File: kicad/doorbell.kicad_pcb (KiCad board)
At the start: 4 copper layers, 40.4 x 47.5 mm, 38 parts, among them J1 USB-C (USB4085), J2 WF26 (6-way screw), K1 G6K-2F-Y 4.5V, K2 G6K-2F-Y 4.5V, Q1 2N7002, Q2 2N7002, SW1 BOOT, SW2 EN, U1 ESP32-C3-WROOM-02-N4, U2 SGM2212-3.3

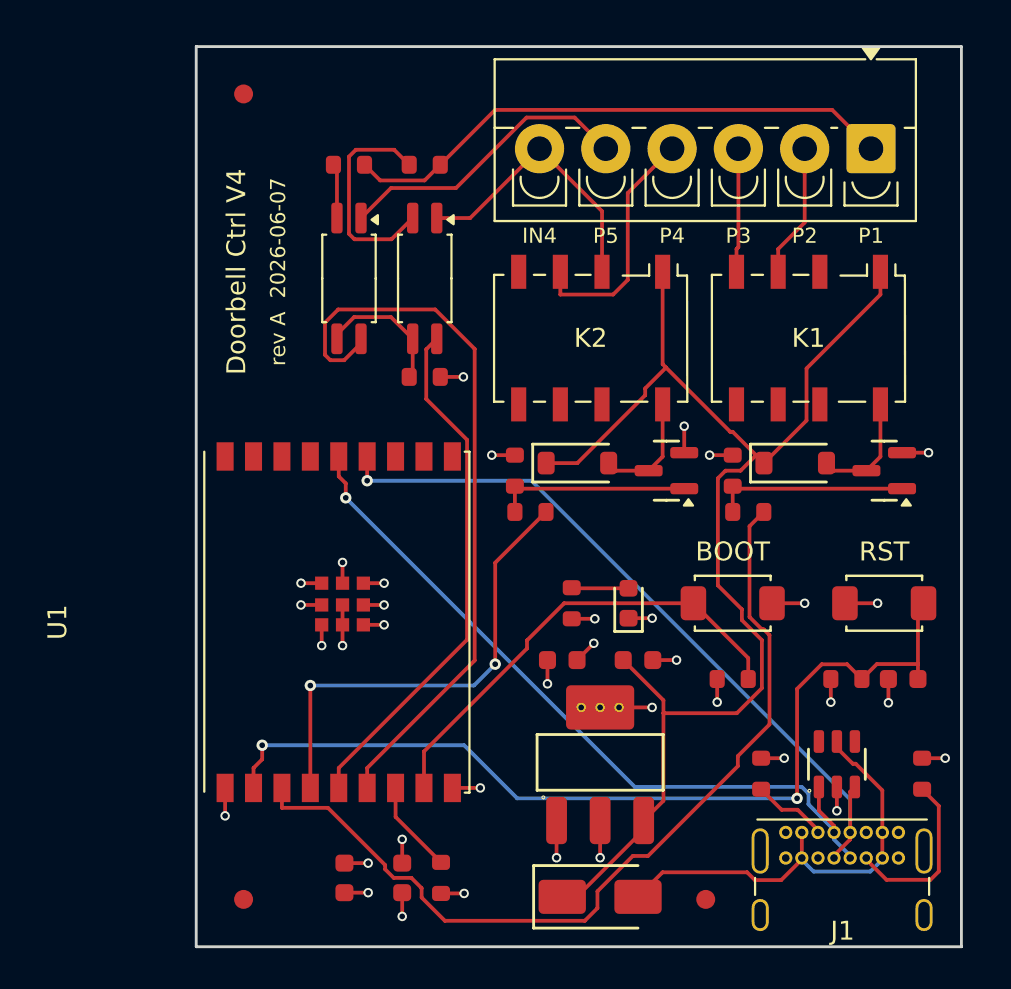
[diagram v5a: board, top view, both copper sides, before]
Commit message: Move bell sense to IO10/IO3 (opto-facing); doc + BOM update for WROOM-02
Reassign OC1_OUT/OC2_OUT from IO6/IO7 to IO10/IO3 so they land on U1's
north castellated row facing the optos: OC1/OC2 now route ~7mm straight
instead of ~25mm around the module. Non-strapping pins; IO6/IO7 freed to
No-Connect. ESPHome updated (House GPIO6->GPIO10, Apartment GPIO7->GPIO3).
Routes 0 unrouted, DRC 0/0, check_pcb PASS.

BOM: U1 LCSC C2838502 (MINI-1) -> C2934560 (WROOM-02-N4).

Docs brought in line with the WROOM-02 swap:
- DESIGN.md: GPIO map, decisions/BOM tables, floorplan, antenna overhang
  (5.9mm), and a 2026-06-08 "changes since review" addendum.
- ORDERING.md: switched the order story to Economic PCBA (no $25/side
  setup; Economic has no >=70mm/rail requirement -- that was Standard);
  updated cost, part-placement table, and the rationale.
- doorbell-v4.yaml + design comments: MINI-1 -> WROOM-02.
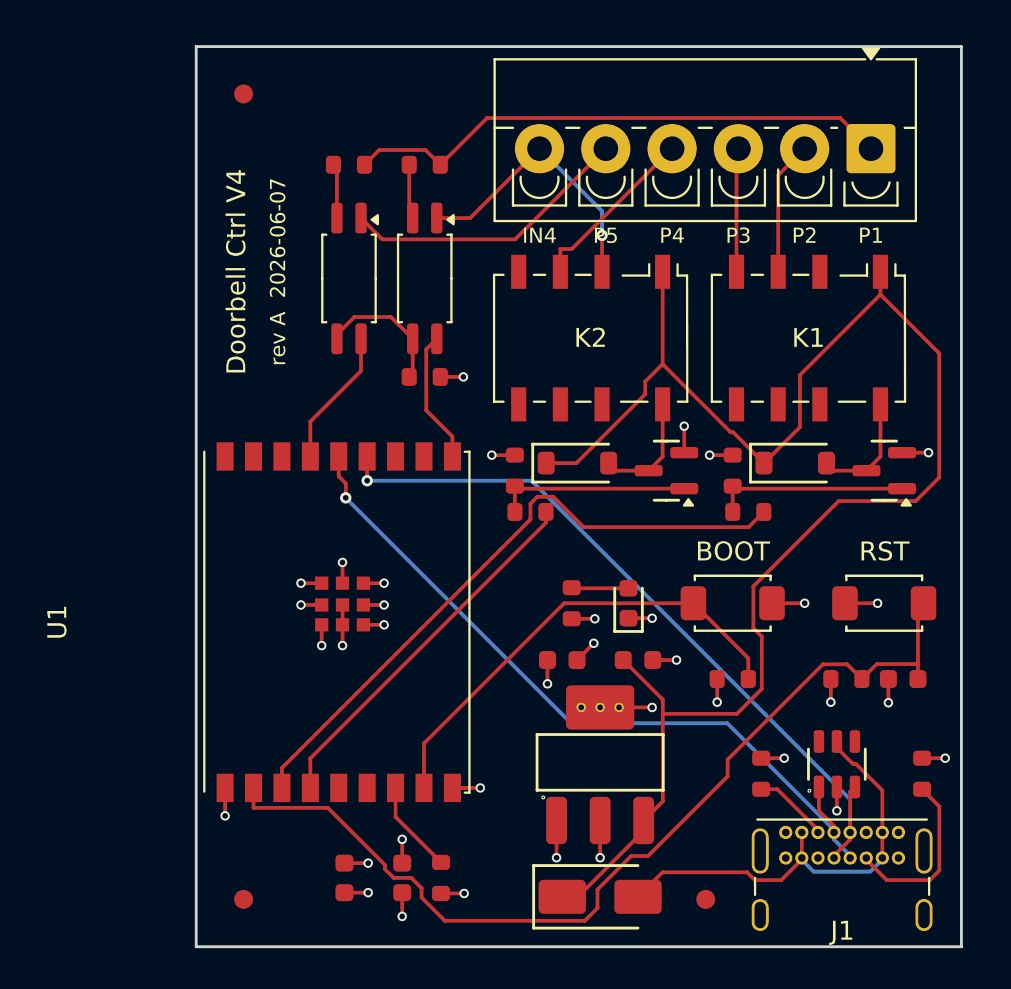
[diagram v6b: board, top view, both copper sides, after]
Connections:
- U1 pad 10: (no net) -> OC1_OUT
- U1 pad 15: (no net) -> OC2_OUT
- U1 pad 5: OC1_OUT -> (no net)
- U1 pad 6: OC2_OUT -> (no net)
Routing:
- net OC2_OUT: track 38.9 -> 7.32 mm
- net OC1_OUT: track 27.6 -> 7.01 mm
- net +5V: track 70.0 -> 84.3 mm
- net GATE1_DRV: track 46.8 -> 33.9 mm
- net OC1_CATH: track 11.7 -> 2.89 mm
- net GATE2_DRV: track 24.8 -> 19.7 mm, vias 2 -> 0
- net P4: track 13.0 -> 9.30 mm
- net EN: track 49.3 -> 50.5 mm, vias 2 -> 0
- net IN_P4: vias 0 -> 1

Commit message: Reverse-engineer WF26 handset; document bus protocol; R_em placement
- wf26/: new standalone KiCad project (ERC-clean) fully tracing the STR
  WF26/G handset internals -- LS1, S1/S2 (DPDT), R1, C1, custom HJR-4102
  relay symbol, 5-way bus. Built via make_wf26.py (kiutils bootstrap).
- DESIGN.md: WF26 internal-trace section + netlist; key finding that P4
  is dual-purpose (Tueruf ring AND Sprechen/Hoeren PTT/on-hook handshake),
  talk=P4<->P2 / listen=P4<->P3, relay-part caveat, open questions.
- docs/HJR4102.PDF: relay datasheet (6-pin DIL SPDT, coil 5/8, COM 1+12).
- kicad/: R_em (R3) re-placed/rotated 180 in gen_pcb.py + regenerated
  board/sch/pdf; add fabrication-toolkit-options.json. Ignore .history/.
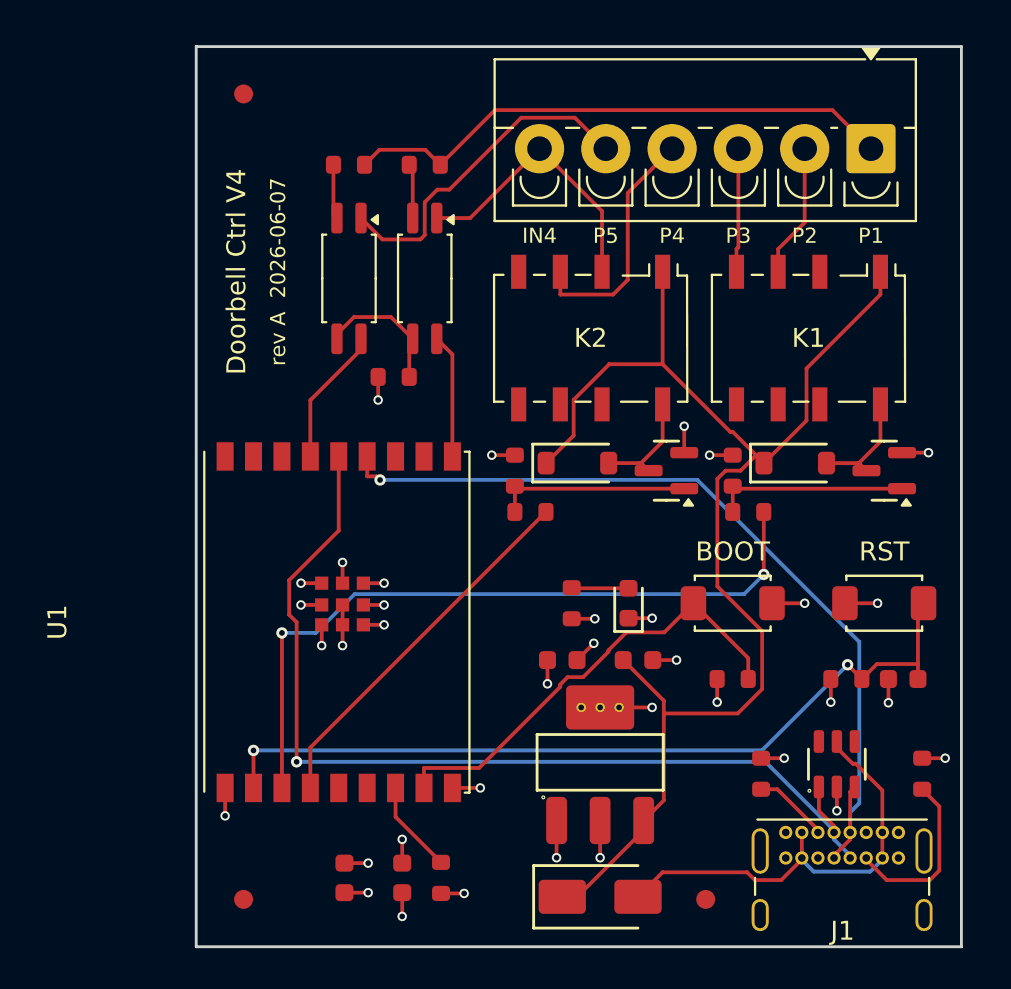
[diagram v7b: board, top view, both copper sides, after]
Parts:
- moved R3 1.64 mm to (5.10, 29.1), turned to 180 degrees
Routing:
- net +5V: track 84.3 -> 70.9 mm
- net USB_DP: track 39.9 -> 51.8 mm
- net EN: track 50.5 -> 43.7 mm, vias 0 -> 2
- net USB_DM: track 39.7 -> 45.1 mm
- net GATE1_DRV: track 33.9 -> 38.2 mm, vias 0 -> 2
- net P4: track 9.30 -> 13.0 mm
- net P5: track 15.4 -> 17.7 mm
- net BOOT: track 24.8 -> 24.2 mm
- net IN_P4: vias 1 -> 0

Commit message: Add R14 (2.2k) in series with K1 door-opener bridge (WF26-faithful)
The genuine WF26 OeT button bridges bus lines 2<->3 through R1 = 2.2 kOhm
(confirmed by colour bands red-red-red-gold), not a dead short -- so it
triggers the TV20/S door opener while only loading the speech pair, not
fully shorting it. Our K1 was dead-shorting 2<->3.

- doorbell_design.py: new R14 (R_ot, 0603 2.2k, LCSC C4190). Door-opener
  bridge re-routed K1.COM=P2, K1.NO -> R14 -> P3 (net OT_BRIDGE).
- gen_schematic.py / gen_pcb.py: R14 placement (right of K1, below J2.P1).
- Regenerated sch (0 ERC errors) + PCB (placed, routed, 0 DRC / 0 unconnected)
  + fab. DESIGN.md updated (pin table, K1 desc, invariant, audio note).
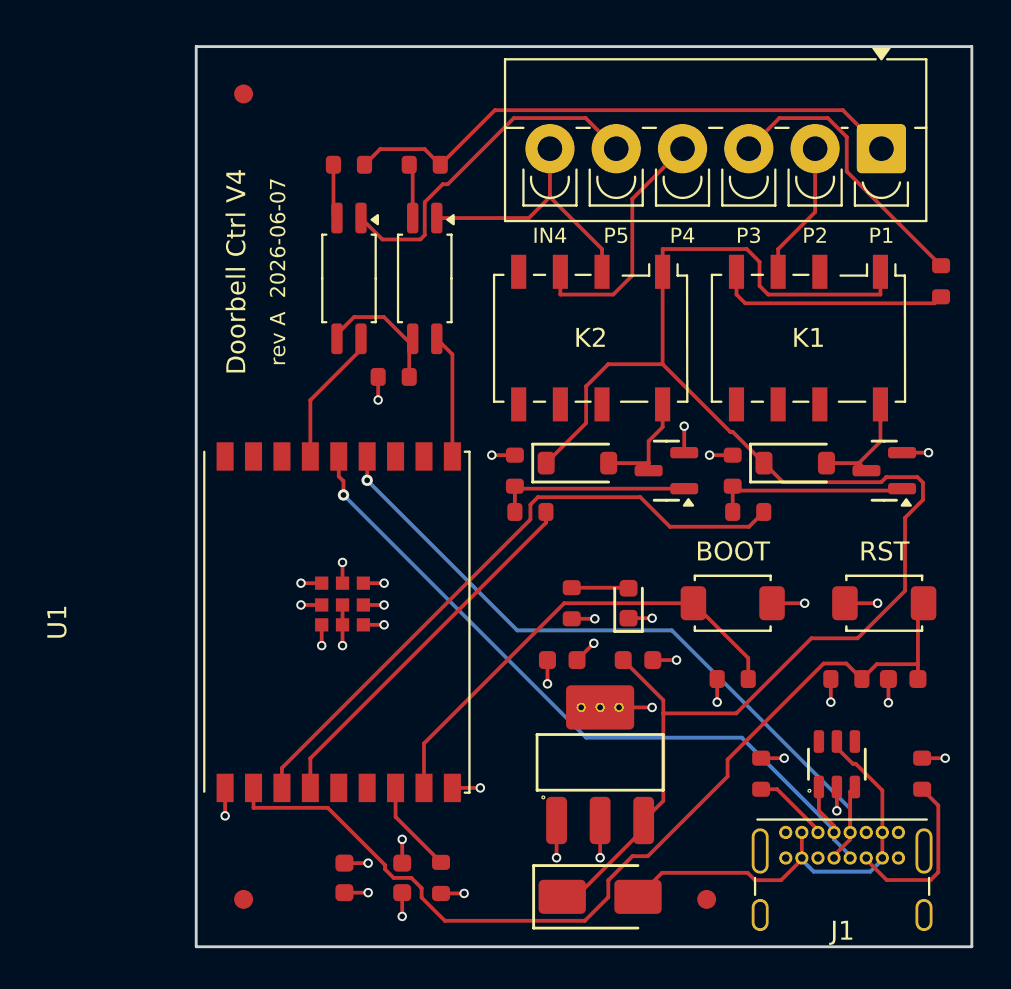
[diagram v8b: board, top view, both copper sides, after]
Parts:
- added R14: 2.2k, R_0603, F.Cu at (34.0, 24.0)
- moved J2 0.55 mm to (30.9, 17.0)
- moved FID3 0.05 mm to (21.6, 56.6)
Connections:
- K1 pad 4: P3 -> OT_BRIDGE
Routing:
- net +5V: track 70.9 -> 84.1 mm
- net OT_BRIDGE: track 0.00 -> 12.3 mm
- net USB_DP: track 51.8 -> 39.9 mm
- net P3: track 6.54 -> 15.1 mm
- net EN: track 43.7 -> 50.5 mm, vias 2 -> 0
- net USB_DM: track 45.1 -> 39.4 mm
- net GATE1_DRV: track 38.2 -> 33.8 mm, vias 2 -> 0
- net IN_P4: track 14.8 -> 14.1 mm
- net BOOT: track 24.2 -> 24.8 mm
- net P1: track 29.4 -> 30.0 mm
- net P5: track 17.7 -> 18.3 mm
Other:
- board size 40.4 x 47.5 mm -> 41 x 47.5 mm
